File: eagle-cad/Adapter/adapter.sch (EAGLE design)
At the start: 19 parts, among them M1 WIREPADSMD5-2,5, M2 WIREPADSMD5-2,5, M3 WIREPADSMD5-2,5, M4 WIREPADSMD5-2,5

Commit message: Worked on Adapter
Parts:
- removed GND2, GND3, GND4, M1, M2, M3, M4, VBAT1, VBAT2, VBAT3, VBAT4: WIREPADSMD5-2,5, wirepad:WIREPADSMD5-2,5
- removed J4: (no value), SparkFun-Connectors:CONN_05NO_SILK
- removed J5: (no value), SparkFun-Connectors:CONN_031X03_NO_SILK
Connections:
- new net SBUS: GND1.P
- net 3V3: no longer J4.4
- net 5V: no longer J5.1
- net GND: no longer GND1.P, GND2.P, GND3.P, GND4.P, J4.5, J5.2
- net M1: no longer M1.P
- net M2: no longer M2.P
- net M3: no longer M3.P
- net M4: no longer M4.P
- net RX1: no longer J5.3
- net SCL: no longer J4.2
- net SDA: no longer J4.1
- net VBAT: no longer VBAT1.P, VBAT2.P, VBAT3.P, VBAT4.P
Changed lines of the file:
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@@
 <?xml version="1.0" encoding="utf-8"?>
 <!DOCTYPE eagle SYSTEM "eagle.dtd">
-<eagle version="9.1.1">
+<eagle version="9.6.2">
 <drawing>
 <settings>
@@
 <part name="J2" library="SparkFun-Connectors" deviceset="CONN_10" device="NO_SILK_PTH_FEMALE"/>
 <part name="J3" library="SparkFun-Connectors" deviceset="CONN_03" device="1X03_NO_SILK"/>
-<part name="J4" library="SparkFun-Connectors" deviceset="CONN_05" device="NO_SILK"/>
-<part name="M4" library="wirepad" deviceset="WIREPAD" device="SMD5-2,5"/>
 <part name="GND1" library="wirepad" deviceset="WIREPAD" device="SMD5-2,5"/>
-<part name="VBAT1" library="wirepad" deviceset="WIREPAD" device="SMD5-2,5"/>
-<part name="M1" library="wirepad" deviceset="WIREPAD" device="SMD5-2,5"/>
-<part name="GND2" library="wirepad" deviceset="WIREPAD" device="SMD5-2,5"/>
-<part name="VBAT2" library="wirepad" deviceset="WIREPAD" device="SMD5-2,5"/>
-<part name="M2" library="wirepad" deviceset="WIREPAD" device="SMD5-2,5"/>
-<part name="GND3" library="wirepad" deviceset="WIREPAD" device="SMD5-2,5"/>
-<part name="VBAT3" library="wirepad" deviceset="WIREPAD" device="SMD5-2,5"/>
-<part name="M3" library="wirepad" deviceset="WIREPAD" device="SMD5-2,5"/>
-<part name="GND4" library="wirepad" deviceset="WIREPAD" device="SMD5-2,5"/>
-<part name="VBAT4" library="wirepad" deviceset="WIREPAD" device="SMD5-2,5"/>
-<part name="J5" library="SparkFun-Connectors" deviceset="CONN_03" device="1X03_NO_SILK"/>
 </parts>
 <sheets>
@@
 </plain>
 <instances>
-<instance part="GND" gate="G$1" x="2.54" y="0" smashed="yes">
-<attribute name="VALUE" x="1.397" y="-3.302" size="1.778" layer="96"/>
-</instance>
+<instance part="GND" gate="G$1" x="2.54" y="0" smashed="yes"/>
 <instance part="VBAT" gate="G$1" x="2.54" y="-12.7" smashed="yes"/>
 <instance part="J1" gate="J1" x="-15.24" y="68.58" smashed="yes">
@@
 <attribute name="NAME" x="-50.8" y="28.448" size="1.778" layer="95" font="vector"/>
 </instance>
-<instance part="J4" gate="G$1" x="-50.8" y="-7.62" smashed="yes">
-<attribute name="VALUE" x="-53.34" y="-17.526" size="1.778" layer="96" font="vector"/>
-<attribute name="NAME" x="-53.34" y="0.508" size="1.778" layer="95" font="vector"/>
-</instance>
-<instance part="M4" gate="G$1" x="2.54" y="-22.86" smashed="yes"/>
 <instance part="GND1" gate="G$1" x="2.54" y="-43.18" smashed="yes"/>
-<instance part="VBAT1" gate="G$1" x="2.54" y="-55.88" smashed="yes"/>
-<instance part="M1" gate="G$1" x="2.54" y="-66.04" smashed="yes"/>
-<instance part="GND2" gate="G$1" x="63.5" y="2.54" smashed="yes"/>
-<instance part="VBAT2" gate="G$1" x="63.5" y="-10.16" smashed="yes"/>
-<instance part="M2" gate="G$1" x="63.5" y="-20.32" smashed="yes"/>
-<instance part="GND3" gate="G$1" x="66.04" y="-43.18" smashed="yes"/>
-<instance part="VBAT3" gate="G$1" x="66.04" y="-55.88" smashed="yes"/>
-<instance part="M3" gate="G$1" x="66.04" y="-66.04" smashed="yes"/>
-<instance part="GND4" gate="G$1" x="2.54" y="-93.98" smashed="yes">
-<attribute name="NAME" x="1.397" y="-92.1258" size="1.778" layer="95"/>
-<attribute name="VALUE" x="1.397" y="-97.282" size="1.778" layer="96"/>
-</instance>
-<instance part="VBAT4" gate="G$1" x="2.54" y="-106.68" smashed="yes">
-<attribute name="NAME" x="1.397" y="-104.8258" size="1.778" layer="95"/>
-<attribute name="VALUE" x="1.397" y="-109.982" size="1.778" layer="96"/>
-</instance>
-<instance part="J5" gate="J$1" x="-35.56" y="-35.56" smashed="yes">
-<attribute name="VALUE" x="-38.1" y="-42.926" size="1.778" layer="96" font="vector"/>
-</instance>
 </instances>
 <busses>
@@
 </segment>
 <segment>
-<pinref part="J4" gate="G$1" pin="5"/>
-<wire x1="-43.18" y1="-2.54" x2="-35.56" y2="-2.54" width="0.1524" layer="91"/>
-<label x="-43.18" y="-2.54" size="1.778" layer="95"/>
-</segment>
-<segment>
-<pinref part="GND4" gate="G$1" pin="P"/>
-<wire x1="5.08" y1="-93.98" x2="15.24" y2="-93.98" width="0.1524" layer="91"/>
-<label x="7.62" y="-93.98" size="1.778" layer="95"/>
-</segment>
-<segment>
 <pinref part="GND" gate="G$1" pin="P"/>
 <wire x1="5.08" y1="0" x2="15.24" y2="0" width="0.1524" layer="91"/>
 <label x="5.08" y="0" size="1.778" layer="95"/>
 </segment>
-<segment>
-<pinref part="GND1" gate="G$1" pin="P"/>
-<wire x1="5.08" y1="-43.18" x2="15.24" y2="-43.18" width="0.1524" layer="91"/>
-<label x="7.62" y="-43.18" size="1.778" layer="95"/>
-</segment>
-<segment>
-<pinref part="GND2" gate="G$1" pin="P"/>
-<wire x1="66.04" y1="2.54" x2="76.2" y2="2.54" width="0.1524" layer="91"/>
-<label x="68.58" y="2.54" size="1.778" layer="95"/>
-</segment>
-<segment>
-<pinref part="GND3" gate="G$1" pin="P"/>
-<wire x1="68.58" y1="-43.18" x2="78.74" y2="-43.18" width="0.1524" layer="91"/>
-<label x="71.12" y="-43.18" size="1.778" layer="95"/>
-</segment>
-<segment>
-<pinref part="J5" gate="J$1" pin="2"/>
-<wire x1="-27.94" y1="-35.56" x2="-20.32" y2="-35.56" width="0.1524" layer="91"/>
-<label x="-27.94" y="-35.56" size="1.778" layer="95"/>
-</segment>
 </net>
 <net name="5V" class="0">
@@
 <label x="-40.64" y="20.32" size="1.778" layer="95"/>
 </segment>
-<segment>
-<pinref part="J5" gate="J$1" pin="1"/>
-<wire x1="-27.94" y1="-38.1" x2="-20.32" y2="-38.1" width="0.1524" layer="91"/>
-<label x="-27.94" y="-38.1" size="1.778" layer="95"/>
-</segment>
 </net>
 <net name="3V3" class="0">
@@
 <label x="-5.08" y="58.42" size="1.778" layer="95"/>
 </segment>
-<segment>
-<pinref part="J4" gate="G$1" pin="4"/>
-<wire x1="-43.18" y1="-5.08" x2="-35.56" y2="-5.08" width="0.1524" layer="91"/>
-<label x="-43.18" y="-5.08" size="1.778" layer="95"/>
-</segment>
 </net>
 <net name="M1" class="0">
@@
 <label x="-5.08" y="73.66" size="1.778" layer="95"/>
 </segment>
-<segment>
-<pinref part="M1" gate="G$1" pin="P"/>
-<wire x1="5.08" y1="-66.04" x2="17.78" y2="-66.04" width="0.1524" layer="91"/>
-<label x="7.62" y="-66.04" size="1.778" layer="95"/>
-</segment>
 </net>
 <net name="M2" class="0">
@@
 <label x="-5.08" y="71.12" size="1.778" layer="95"/>
 </segment>
-<segment>
-<pinref part="M2" gate="G$1" pin="P"/>
-<wire x1="66.04" y1="-20.32" x2="78.74" y2="-20.32" width="0.1524" layer="91"/>
-<label x="68.58" y="-20.32" size="1.778" layer="95"/>
-</segment>
 </net>
 <net name="M3" class="0">
@@
 <label x="-5.08" y="68.58" size="1.778" layer="95"/>
 </segment>
-<segment>
-<pinref part="M3" gate="G$1" pin="P"/>
-<wire x1="68.58" y1="-66.04" x2="81.28" y2="-66.04" width="0.1524" layer="91"/>
-<label x="71.12" y="-66.04" size="1.778" layer="95"/>
-</segment>
 </net>
 <net name="M4" class="0">
@@
 <label x="-5.08" y="66.04" size="1.778" layer="95"/>
 </segment>
-<segment>
-<pinref part="M4" gate="G$1" pin="P"/>
-<wire x1="5.08" y1="-22.86" x2="17.78" y2="-22.86" width="0.1524" layer="91"/>
-<label x="5.08" y="-22.86" size="1.778" layer="95"/>
-</segment>
 </net>
 <net name="SCL" class="0">
-<segment>
-<pinref part="J4" gate="G$1" pin="2"/>
-<wire x1="-43.18" y1="-10.16" x2="-35.56" y2="-10.16" width="0.1524" layer="91"/>
-<label x="-43.18" y="-10.16" size="1.778" layer="95"/>
-</segment>
 <segment>
 <pinref part="J2" gate="J1" pin="5"/>
@@
 <net name="SDA" class="0">
 <segment>
-<pinref part="J4" gate="G$1" pin="1"/>
-<wire x1="-43.18" y1="-12.7" x2="-35.56" y2="-12.7" width="0.1524" layer="91"/>
-<label x="-43.18" y="-12.7" size="1.778" layer="95"/>
-</segment>
-<segment>
 <pinref part="J2" gate="J1" pin="6"/>
 <wire x1="20.32" y1="63.5" x2="25.4" y2="63.5" width="0.1524" layer="91"/>
@@
 <net name="RX1" class="0">
 <segment>
-<pinref part="J5" gate="J$1" pin="3"/>
-<wire x1="-27.94" y1="-33.02" x2="-20.32" y2="-33.02" width="0.1524" layer="91"/>
-<label x="-27.94" y="-33.02" size="1.778" layer="95"/>
-</segment>
-<segment>
 <pinref part="J2" gate="J1" pin="7"/>
 <wire x1="20.32" y1="66.04" x2="25.4" y2="66.04" width="0.1524" layer="91"/>
@@
 </segment>
 <segment>
-<pinref part="VBAT4" gate="G$1" pin="P"/>
-<wire x1="5.08" y1="-106.68" x2="15.24" y2="-106.68" width="0.1524" layer="91"/>
-<label x="7.62" y="-106.68" size="1.778" layer="95"/>
-</segment>
-<segment>
 <pinref part="VBAT" gate="G$1" pin="P"/>
 <wire x1="5.08" y1="-12.7" x2="15.24" y2="-12.7" width="0.1524" layer="91"/>
 <label x="5.08" y="-12.7" size="1.778" layer="95"/>
 </segment>
-<segment>
-<pinref part="VBAT1" gate="G$1" pin="P"/>
-<wire x1="5.08" y1="-55.88" x2="15.24" y2="-55.88" width="0.1524" layer="91"/>
-<label x="7.62" y="-55.88" size="1.778" layer="95"/>
-</segment>
-<segment>
-<pinref part="VBAT2" gate="G$1" pin="P"/>
-<wire x1="66.04" y1="-10.16" x2="76.2" y2="-10.16" width="0.1524" layer="91"/>
-<label x="68.58" y="-10.16" size="1.778" layer="95"/>
-</segment>
-<segment>
-<pinref part="VBAT3" gate="G$1" pin="P"/>
-<wire x1="68.58" y1="-55.88" x2="78.74" y2="-55.88" width="0.1524" layer="91"/>
-<label x="71.12" y="-55.88" size="1.778" layer="95"/>
-</segment>
 </net>
 <net name="TX1" class="0">
@@
 </segment>
 </net>
+<net name="SBUS" class="0">
+<segment>
+<pinref part="GND1" gate="G$1" pin="P"/>
+<wire x1="5.08" y1="-43.18" x2="15.24" y2="-43.18" width="0.1524" layer="91"/>
+<label x="5.08" y="-43.18" size="1.778" layer="95"/>
+</segment>
+</net>

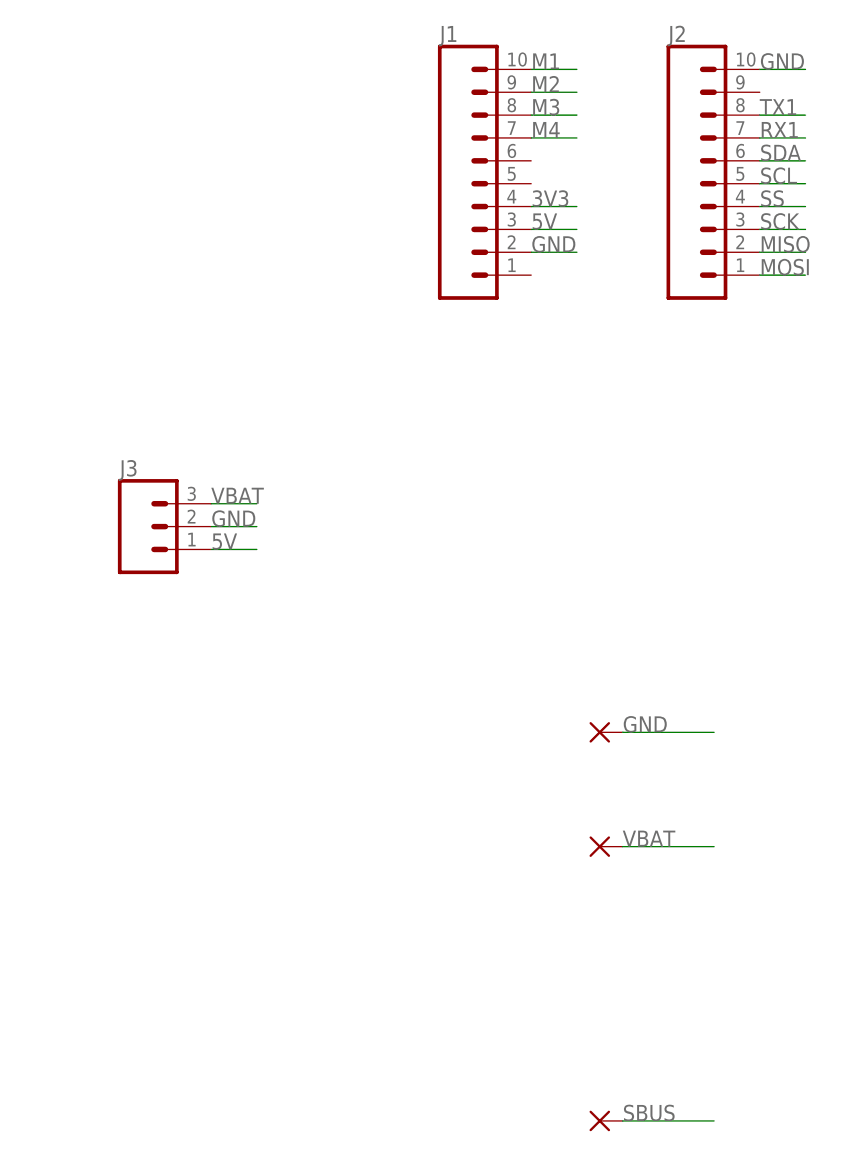
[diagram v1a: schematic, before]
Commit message: Finished Taranis X-Lite adapter design
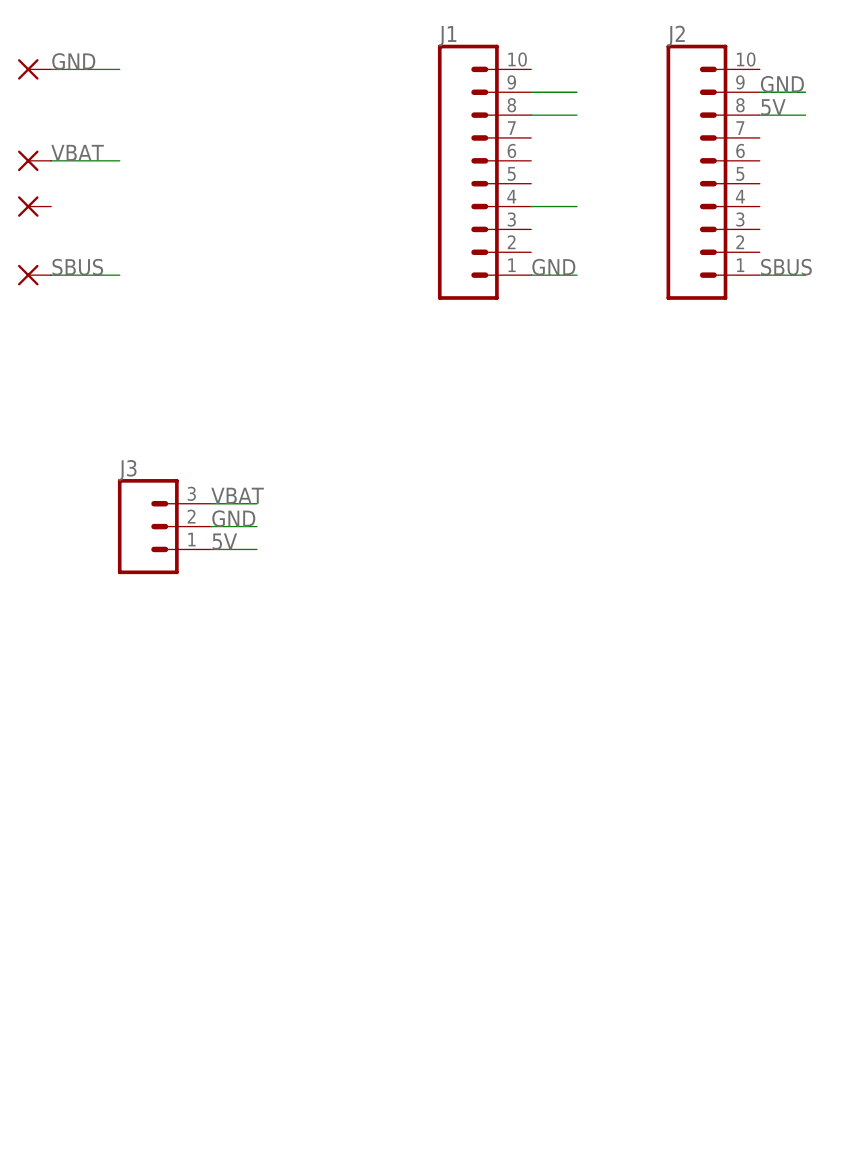
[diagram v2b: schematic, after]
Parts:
- removed GND1: WIREPADSMD5-2,5, wirepad:WIREPADSMD5-2,5
- added PAD1, SBUS: (no value), wirepad:SMD2
- GND, VBAT: value WIREPADSMD5-2,5 -> (none); device wirepad:WIREPADSMD5-2,5 -> wirepad:SMD2
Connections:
- removed net M1: J1.10
- removed net M4: J1.7
- removed net MISO: J2.2
- removed net MOSI: J2.1
- removed net RX1: J2.7
- removed net SCK: J2.3
- removed net SCL: J2.5
- removed net SDA: J2.6
- removed net SS: J2.4
- removed net TX1: J2.8
- net 5V: now also J2.8; no longer J1.3
- net GND: now also J1.1, J2.9; no longer J1.2, J2.10
- net SBUS: now also J2.1, SBUS.P; no longer GND1.P
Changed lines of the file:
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@@
 <?xml version="1.0" encoding="utf-8"?>
 <!DOCTYPE eagle SYSTEM "eagle.dtd">
-<eagle version="9.6.2">
+<eagle version="9.1.1">
 <drawing>
 <settings>
@@
 </classes>
 <parts>
-<part name="GND" library="wirepad" deviceset="WIREPAD" device="SMD5-2,5"/>
-<part name="VBAT" library="wirepad" deviceset="WIREPAD" device="SMD5-2,5"/>
 <part name="J1" library="SparkFun-Connectors" deviceset="CONN_10" device="NO_SILK_PTH_FEMALE"/>
 <part name="J2" library="SparkFun-Connectors" deviceset="CONN_10" device="NO_SILK_PTH_FEMALE"/>
 <part name="J3" library="SparkFun-Connectors" deviceset="CONN_03" device="1X03_NO_SILK"/>
-<part name="GND1" library="wirepad" deviceset="WIREPAD" device="SMD5-2,5"/>
+<part name="GND" library="wirepad" deviceset="SMD2" device=""/>
+<part name="VBAT" library="wirepad" deviceset="SMD2" device=""/>
+<part name="SBUS" library="wirepad" deviceset="SMD2" device=""/>
+<part name="PAD1" library="wirepad" deviceset="SMD2" device=""/>
 </parts>
 <sheets>
@@
 </plain>
 <instances>
-<instance part="GND" gate="G$1" x="2.54" y="0" smashed="yes"/>
-<instance part="VBAT" gate="G$1" x="2.54" y="-12.7" smashed="yes"/>
 <instance part="J1" gate="J1" x="-15.24" y="68.58" smashed="yes">
 <attribute name="VALUE" x="-15.24" y="45.974" size="1.778" layer="96" font="vector"/>
@@
 <attribute name="NAME" x="-50.8" y="28.448" size="1.778" layer="95" font="vector"/>
 </instance>
-<instance part="GND1" gate="G$1" x="2.54" y="-43.18" smashed="yes"/>
+<instance part="GND" gate="1" x="-60.96" y="73.66" smashed="yes">
+<attribute name="VALUE" x="-62.103" y="70.358" size="1.778" layer="96"/>
+</instance>
+<instance part="VBAT" gate="1" x="-60.96" y="63.5" smashed="yes">
+<attribute name="VALUE" x="-62.103" y="60.198" size="1.778" layer="96"/>
+</instance>
+<instance part="SBUS" gate="1" x="-60.96" y="50.8" smashed="yes">
+<attribute name="VALUE" x="-62.103" y="47.498" size="1.778" layer="96"/>
+</instance>
+<instance part="PAD1" gate="1" x="-60.96" y="58.42" smashed="yes">
+<attribute name="VALUE" x="-62.103" y="55.118" size="1.778" layer="96"/>
+</instance>
 </instances>
 <busses>
@@
 <net name="GND" class="0">
 <segment>
-<pinref part="J1" gate="J1" pin="2"/>
-<wire x1="-5.08" y1="53.34" x2="0" y2="53.34" width="0.1524" layer="91"/>
-<label x="-5.08" y="53.34" size="1.778" layer="95"/>
-</segment>
-<segment>
-<pinref part="J2" gate="J1" pin="10"/>
-<wire x1="20.32" y1="73.66" x2="25.4" y2="73.66" width="0.1524" layer="91"/>
-<label x="20.32" y="73.66" size="1.778" layer="95"/>
-</segment>
-<segment>
 <pinref part="J3" gate="J$1" pin="2"/>
 <wire x1="-40.64" y1="22.86" x2="-35.56" y2="22.86" width="0.1524" layer="91"/>
@@
 </segment>
 <segment>
-<pinref part="GND" gate="G$1" pin="P"/>
-<wire x1="5.08" y1="0" x2="15.24" y2="0" width="0.1524" layer="91"/>
-<label x="5.08" y="0" size="1.778" layer="95"/>
+<pinref part="GND" gate="1" pin="P"/>
+<wire x1="-58.42" y1="73.66" x2="-50.8" y2="73.66" width="0.1524" layer="91"/>
+<label x="-58.42" y="73.66" size="1.778" layer="95"/>
+</segment>
+<segment>
+<pinref part="J1" gate="J1" pin="1"/>
+<wire x1="-5.08" y1="50.8" x2="0" y2="50.8" width="0.1524" layer="91"/>
+<label x="-5.08" y="50.8" size="1.778" layer="95"/>
+</segment>
+<segment>
+<pinref part="J2" gate="J1" pin="9"/>
+<wire x1="20.32" y1="71.12" x2="25.4" y2="71.12" width="0.1524" layer="91"/>
+<label x="20.32" y="71.12" size="1.778" layer="95"/>
 </segment>
 </net>
 <net name="5V" class="0">
-<segment>
-<pinref part="J1" gate="J1" pin="3"/>
-<wire x1="-5.08" y1="55.88" x2="0" y2="55.88" width="0.1524" layer="91"/>
-<label x="-5.08" y="55.88" size="1.778" layer="95"/>
-</segment>
 <segment>
 <pinref part="J3" gate="J$1" pin="1"/>
@@
 <label x="-40.64" y="20.32" size="1.778" layer="95"/>
 </segment>
+<segment>
+<pinref part="J2" gate="J1" pin="8"/>
+<wire x1="20.32" y1="68.58" x2="25.4" y2="68.58" width="0.1524" layer="91"/>
+<label x="20.32" y="68.58" size="1.778" layer="95"/>
+</segment>
 </net>
 <net name="3V3" class="0">
@@
 <pinref part="J1" gate="J1" pin="4"/>
 <wire x1="-5.08" y1="58.42" x2="0" y2="58.42" width="0.1524" layer="91"/>
-<label x="-5.08" y="58.42" size="1.778" layer="95"/>
-</segment>
-</net>
-<net name="M1" class="0">
-<segment>
-<pinref part="J1" gate="J1" pin="10"/>
-<wire x1="-5.08" y1="73.66" x2="0" y2="73.66" width="0.1524" layer="91"/>
-<label x="-5.08" y="73.66" size="1.778" layer="95"/>
 </segment>
 </net>
@@
 <pinref part="J1" gate="J1" pin="9"/>
 <wire x1="-5.08" y1="71.12" x2="0" y2="71.12" width="0.1524" layer="91"/>
-<label x="-5.08" y="71.12" size="1.778" layer="95"/>
 </segment>
 </net>
@@
 <pinref part="J1" gate="J1" pin="8"/>
 <wire x1="-5.08" y1="68.58" x2="0" y2="68.58" width="0.1524" layer="91"/>
-<label x="-5.08" y="68.58" size="1.778" layer="95"/>
-</segment>
-</net>
-<net name="M4" class="0">
-<segment>
-<pinref part="J1" gate="J1" pin="7"/>
-<wire x1="-5.08" y1="66.04" x2="0" y2="66.04" width="0.1524" layer="91"/>
-<label x="-5.08" y="66.04" size="1.778" layer="95"/>
-</segment>
-</net>
-<net name="SCL" class="0">
-<segment>
-<pinref part="J2" gate="J1" pin="5"/>
-<wire x1="20.32" y1="60.96" x2="25.4" y2="60.96" width="0.1524" layer="91"/>
-<label x="20.32" y="60.96" size="1.778" layer="95"/>
-</segment>
-</net>
-<net name="SDA" class="0">
-<segment>
-<pinref part="J2" gate="J1" pin="6"/>
-<wire x1="20.32" y1="63.5" x2="25.4" y2="63.5" width="0.1524" layer="91"/>
-<label x="20.32" y="63.5" size="1.778" layer="95"/>
-</segment>
-</net>
-<net name="SS" class="0">
-<segment>
-<pinref part="J2" gate="J1" pin="4"/>
-<wire x1="20.32" y1="58.42" x2="25.4" y2="58.42" width="0.1524" layer="91"/>
-<label x="20.32" y="58.42" size="1.778" layer="95"/>
-</segment>
-</net>
-<net name="SCK" class="0">
-<segment>
-<pinref part="J2" gate="J1" pin="3"/>
-<wire x1="20.32" y1="55.88" x2="25.4" y2="55.88" width="0.1524" layer="91"/>
-<label x="20.32" y="55.88" size="1.778" layer="95"/>
-</segment>
-</net>
-<net name="MISO" class="0">
-<segment>
-<pinref part="J2" gate="J1" pin="2"/>
-<wire x1="20.32" y1="53.34" x2="25.4" y2="53.34" width="0.1524" layer="91"/>
-<label x="20.32" y="53.34" size="1.778" layer="95"/>
-</segment>
-</net>
-<net name="MOSI" class="0">
+</segment>
+</net>
+<net name="VBAT" class="0">
+<segment>
+<pinref part="J3" gate="J$1" pin="3"/>
+<wire x1="-40.64" y1="25.4" x2="-35.56" y2="25.4" width="0.1524" layer="91"/>
+<label x="-40.64" y="25.4" size="1.778" layer="95"/>
+</segment>
+<segment>
+<pinref part="VBAT" gate="1" pin="P"/>
+<wire x1="-58.42" y1="63.5" x2="-50.8" y2="63.5" width="0.1524" layer="91"/>
+<label x="-58.42" y="63.5" size="1.778" layer="95"/>
+</segment>
+</net>
+<net name="SBUS" class="0">
+<segment>
+<pinref part="SBUS" gate="1" pin="P"/>
+<wire x1="-58.42" y1="50.8" x2="-50.8" y2="50.8" width="0.1524" layer="91"/>
+<label x="-58.42" y="50.8" size="1.778" layer="95"/>
+</segment>
 <segment>
 <pinref part="J2" gate="J1" pin="1"/>
@@
 </segment>
 </net>
-<net name="RX1" class="0">
-<segment>
-<pinref part="J2" gate="J1" pin="7"/>
-<wire x1="20.32" y1="66.04" x2="25.4" y2="66.04" width="0.1524" layer="91"/>
-<label x="20.32" y="66.04" size="1.778" layer="95"/>
-</segment>
-</net>
-<net name="VBAT" class="0">
-<segment>
-<pinref part="J3" gate="J$1" pin="3"/>
-<wire x1="-40.64" y1="25.4" x2="-35.56" y2="25.4" width="0.1524" layer="91"/>
-<label x="-40.64" y="25.4" size="1.778" layer="95"/>
-</segment>
-<segment>
-<pinref part="VBAT" gate="G$1" pin="P"/>
-<wire x1="5.08" y1="-12.7" x2="15.24" y2="-12.7" width="0.1524" layer="91"/>
-<label x="5.08" y="-12.7" size="1.778" layer="95"/>
-</segment>
-</net>
-<net name="TX1" class="0">
-<segment>
-<pinref part="J2" gate="J1" pin="8"/>
-<wire x1="20.32" y1="68.58" x2="25.4" y2="68.58" width="0.1524" layer="91"/>
-<label x="20.32" y="68.58" size="1.778" layer="95"/>
-</segment>
-</net>
-<net name="SBUS" class="0">
-<segment>
-<pinref part="GND1" gate="G$1" pin="P"/>
-<wire x1="5.08" y1="-43.18" x2="15.24" y2="-43.18" width="0.1524" layer="91"/>
-<label x="5.08" y="-43.18" size="1.778" layer="95"/>
-</segment>
-</net>
